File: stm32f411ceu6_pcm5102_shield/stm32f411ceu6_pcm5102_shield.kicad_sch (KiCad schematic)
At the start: 32 parts, among them J1 AudioJack3_Ground_SwitchTR, U1 PCM5102A, U2 SW_DPDT_XLX, U3 SW_DPDT_XLX, U4 SW_DPDT_XLX, U5 SW_DPDT_XLX, U6 SW_DPDT_XLX, U7 HT7533-1

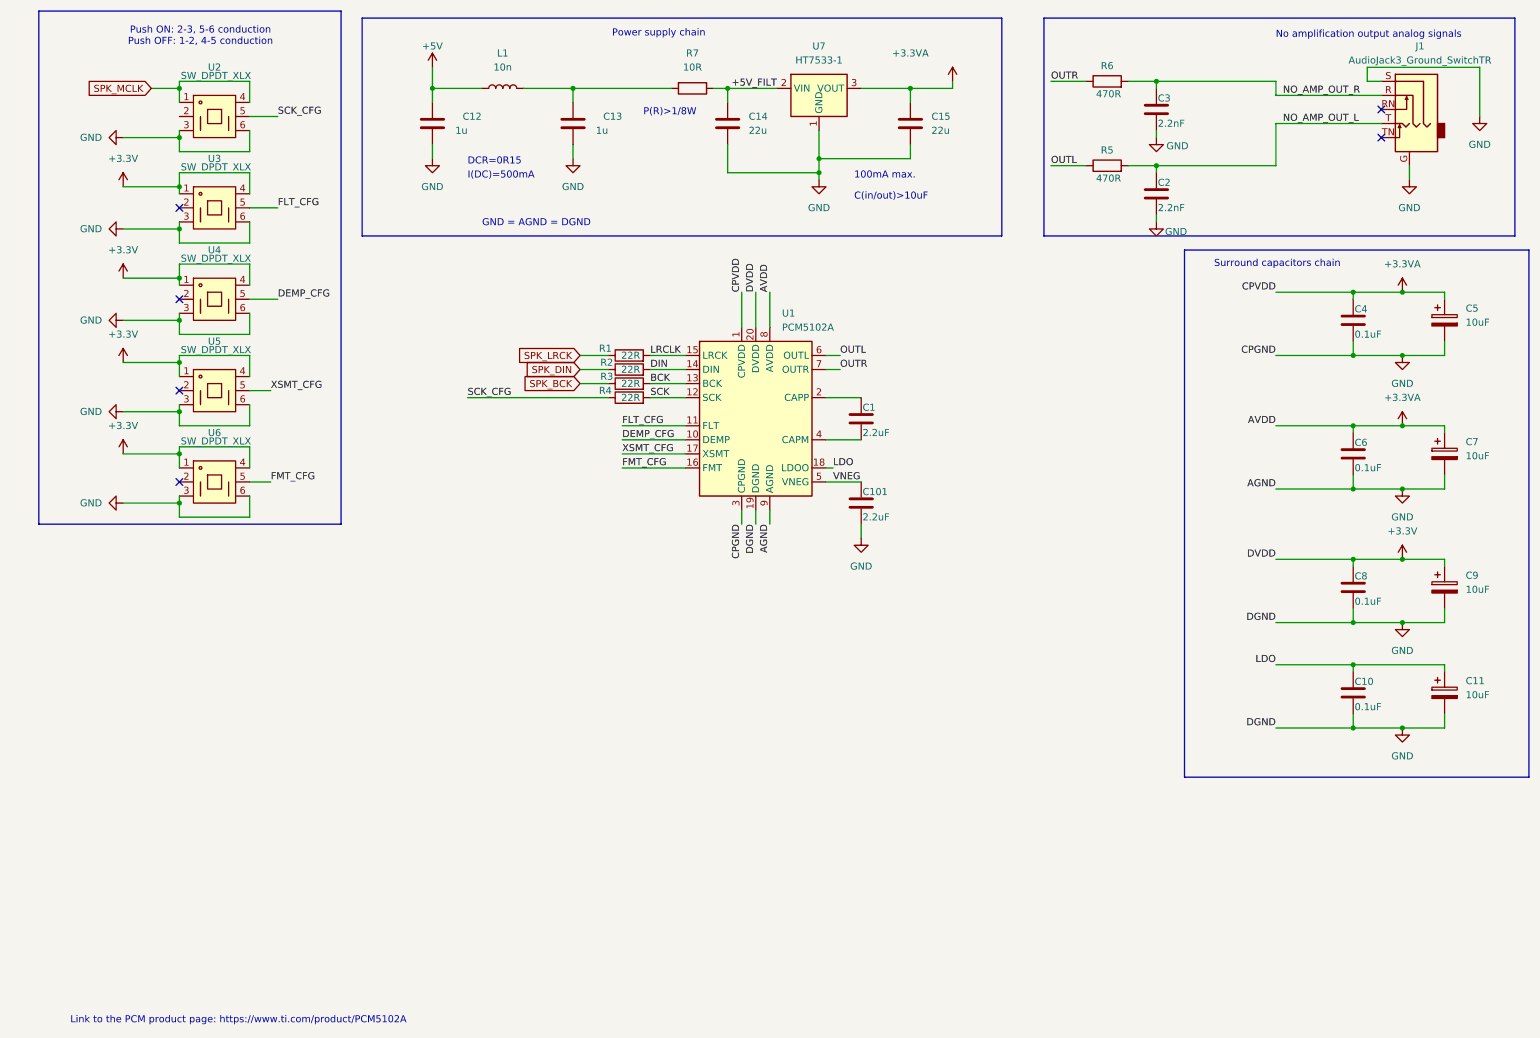
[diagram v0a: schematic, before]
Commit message: Headphone amplifier, black pill footprint & symbol
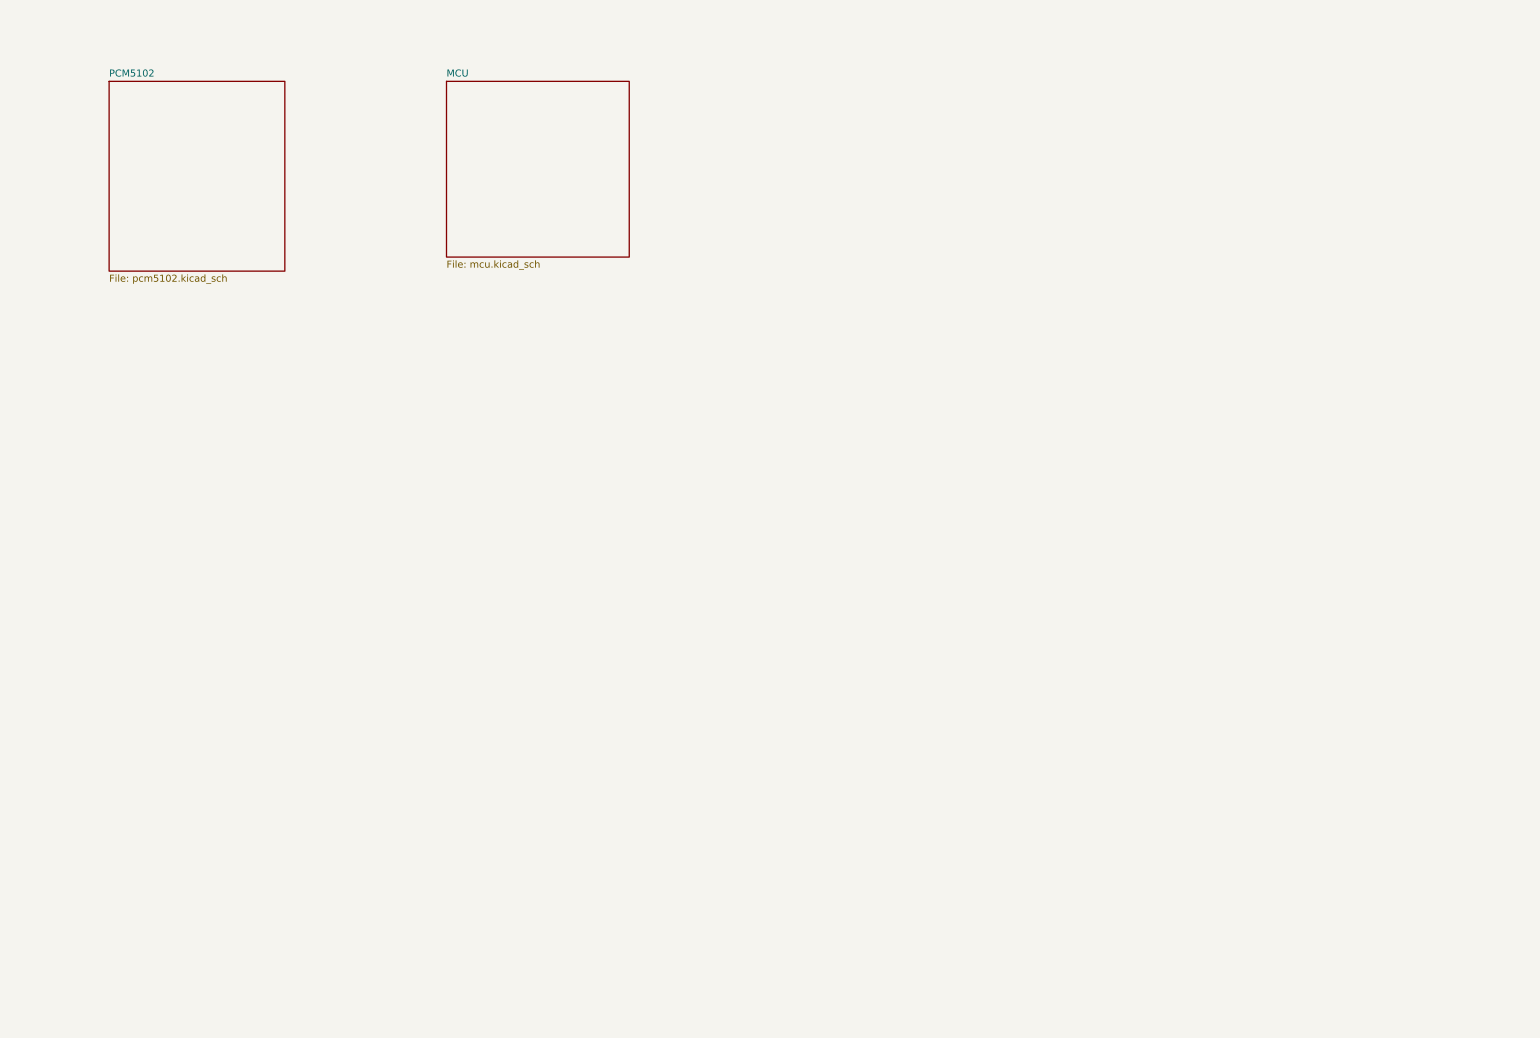
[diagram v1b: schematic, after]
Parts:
- removed C1, C101: 2.2uF, symbol Device:C
- removed C10, C4, C6, C8: 0.1uF, symbol Device:C
- removed C11, C5, C7, C9: 10uF, symbol Device:C_Polarized
- removed C12, C13: 1u, Capacitor_SMD:C_0603_1608Metric, symbol Device:C
- removed C14, C15: 22u, Capacitor_SMD:C_0805_2012Metric, symbol Device:C
- removed C2, C3: 2.2nF, symbol Device:C
- removed J1: AudioJack3_Ground_SwitchTR, Connector_Audio:Jack_3.5mm_PJ311_Horizontal, symbol Connector_Audio:AudioJack3_Ground_SwitchTR
- removed L1: 10n, Inductor_SMD:L_0402_1005Metric, symbol Device:L
- removed R1, R2, R3, R4: 22R, symbol Device:R
- removed R5, R6: 470R, symbol Device:R
- removed R7: 10R, Resistor_SMD:R_0805_2012Metric, symbol Device:R
- removed U1: PCM5102A, Package_SO:TSSOP-20_4.4x6.5mm_P0.65mm, symbol Audio:PCM5102A
- removed U2, U3, U4, U5, U6: SW_DPDT_XLX, stm32f401_pcm5102_shiled_lib:SW_DPDT_XLX, symbol stm32f401_pcm5102_shiled_lib:SW_DPDT_XLX
- removed U7: HT7533-1, Package_TO_SOT_SMD:SOT-89-3, symbol Regulator_Linear:HT75xx-1-SOT89
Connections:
- no-connect marks 6 -> 0
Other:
- added sheet MCU (mcu.kicad_sch)
- added sheet PCM5102 (pcm5102.kicad_sch)
- note removed: "100mA max."
- note removed: "C(in/out)>10uF"
- note removed: "DCR=0R15"
- note removed: "GND = AGND = DGND"
- note removed: "I(DC)=500mA"
- note removed: "Link to the PCM product page: https://www.ti.com/product/PCM5102A"
- note removed: "No amplification output analog signals"
- note removed: "P(R)>1/8W"
- note removed: "Power supply chain"
- note removed: "Push ON: 2-3, 5-6 conduction Push OFF: 1-2, 4-5 conduction"
- note removed: "Surround capacitors chain"

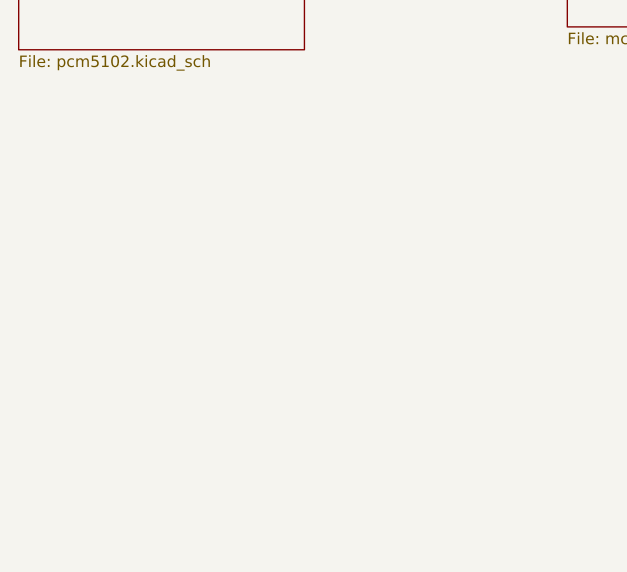
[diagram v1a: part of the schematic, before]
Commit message: Headphone jack detection
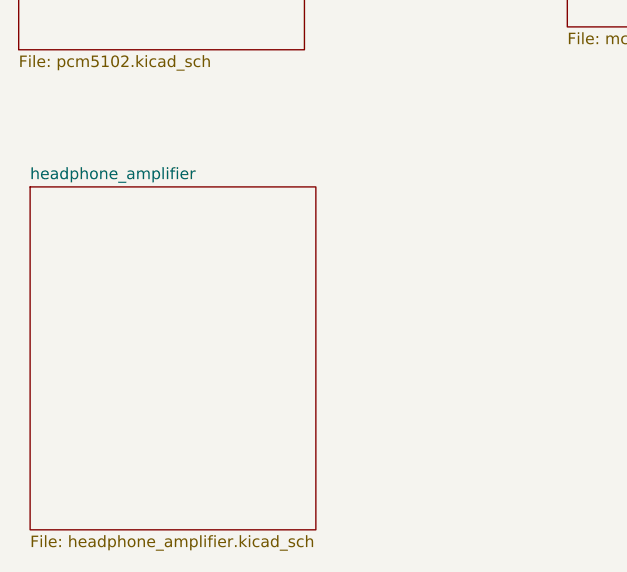
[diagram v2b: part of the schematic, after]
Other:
- added sheet headphone_amplifier (headphone_amplifier.kicad_sch)
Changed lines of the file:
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@@
 	(paper "A4")
+	(sheet
+		(at 26.67 74.93)
+		(size 31.75 38.1)
+		(fields_autoplaced yes)
+		(stroke
+			(width 0.1524)
+			(type solid)
+		)
+		(fill
+			(color 0 0 0 0.0000)
+		)
+		(property "Sheetname" "headphone_amplifier"
+			(at 26.67 74.2184 0)
+			(effects
+				(font
+					(size 1.27 1.27)
+				)
+				(justify left bottom)
+			)
+		)
+		(property "Sheetfile" "headphone_amplifier.kicad_sch"
+			(at 26.67 113.6146 0)
+			(effects
+				(font
+					(size 1.27 1.27)
+				)
+				(justify left top)
+			)
+		)
+		(instances
+			(project "stm32f411ceu6_pcm5102_shield"
+				(path "/aeaad843-2b7c-40e9-bb1d-8d1f5e5d5206"
+					(page "4")
+				)
+			)
+		)
+	)
 	(sheet
 		(at 86.36 25.4)

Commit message: Board outline
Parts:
- added H1, H2, H3, H4: MountingHole, MountingHole:MountingHole_3.2mm_M3, symbol Mechanical:MountingHole
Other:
- note added: "Mounting Holes (M3)"
